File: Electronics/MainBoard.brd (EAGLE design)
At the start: 160 x 100 mm, 10 parts, among them J1 1X2-3.5MM

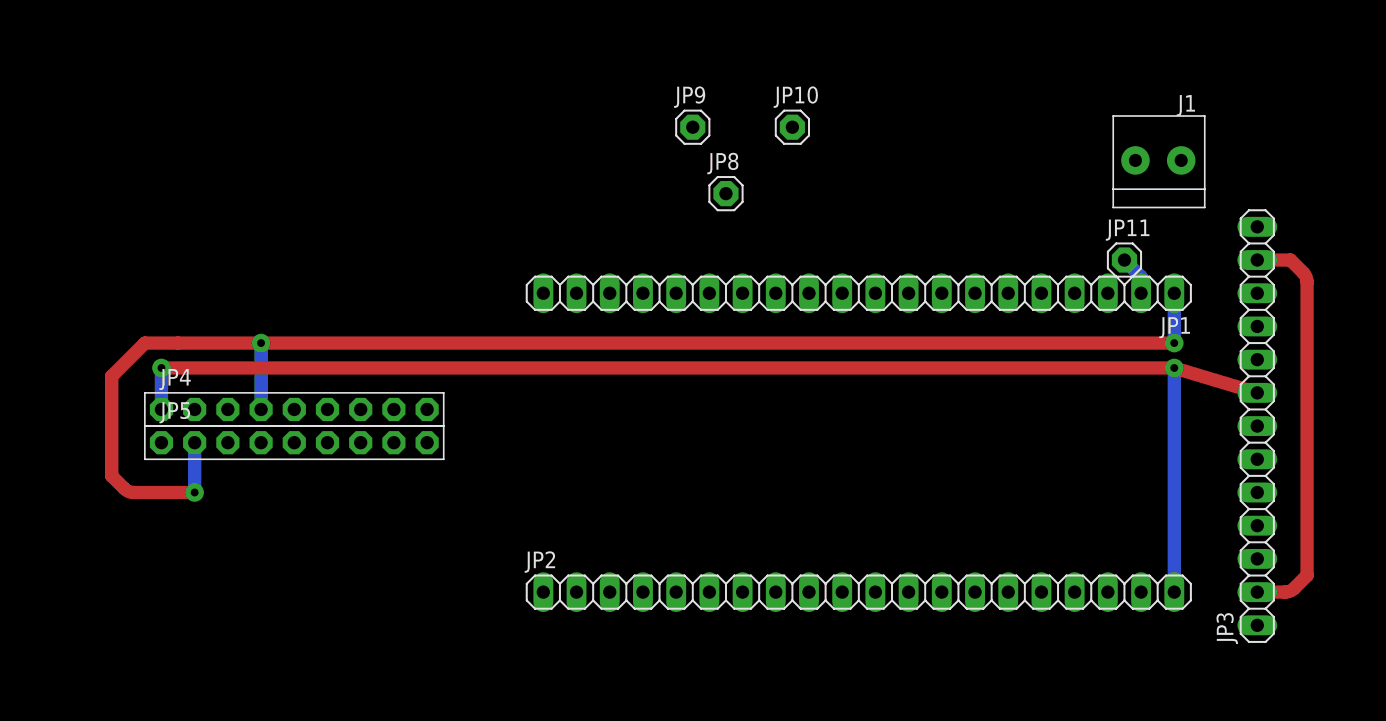
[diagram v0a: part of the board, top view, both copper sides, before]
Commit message: power routed
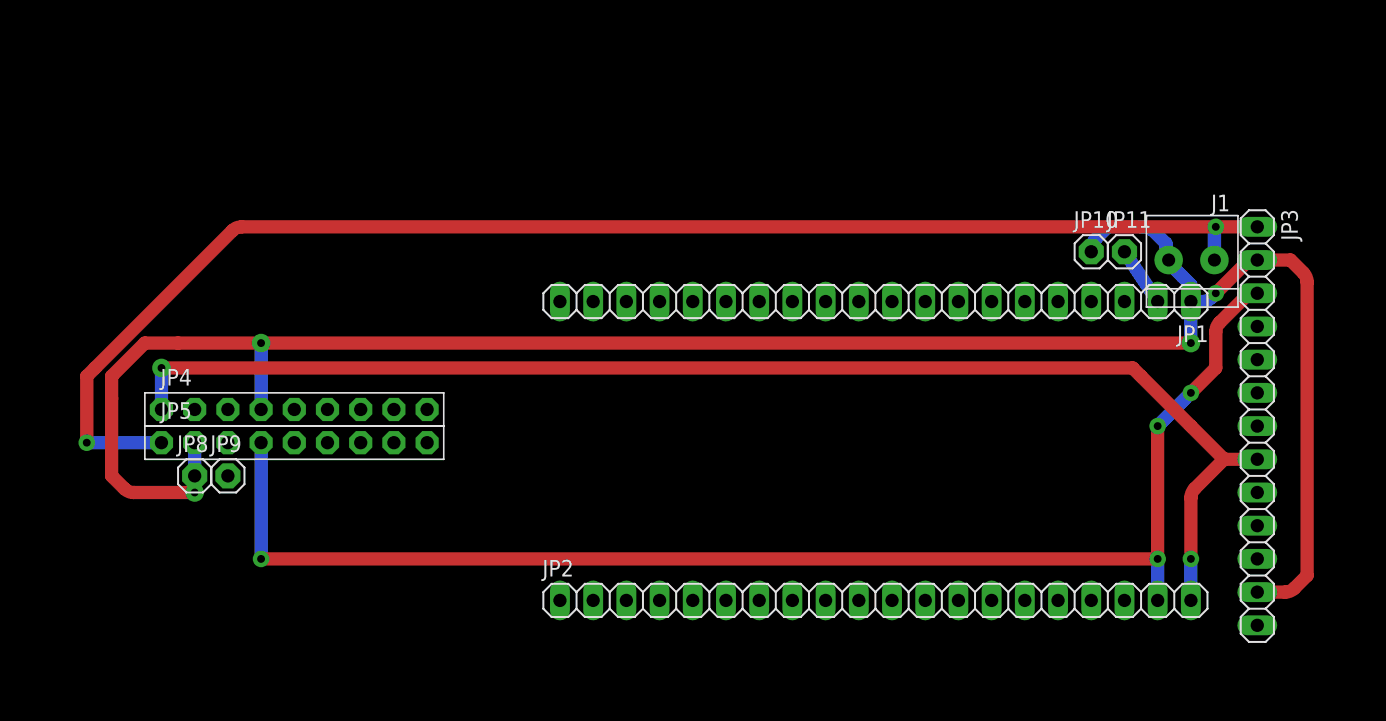
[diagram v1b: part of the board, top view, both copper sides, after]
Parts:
- moved JP8 46.0 mm to (30.5, 47.0)
- moved JP9 44.4 mm to (33.0, 47.0)
- moved JP10 24.8 mm to (99.1, 64.1)
- moved J1 8.03 mm to (106.7, 63.5)
- moved JP1 1.42 mm to (82.5, 60.3)
- moved JP2 1.42 mm to (82.5, 37.5)
- moved JP11 0.64 mm to (101.6, 64.1)
- turned JP3 to 270 degrees
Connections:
- net 8V: now also J1.1
- net GND: now also JP10.1, JP8.1
- net VIN_DIS: now also JP9.1
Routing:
- net 8V: track 0.00 -> 110.1 mm, vias 0 -> 2
- net 5V: track 0.00 -> 104.4 mm, vias 0 -> 4
- net GND: track 140.9 -> 161.5 mm, vias 3 -> 4
- net 3.3V: track 104.4 -> 101.7 mm
- net VIN: track 3.07 -> 4.58 mm

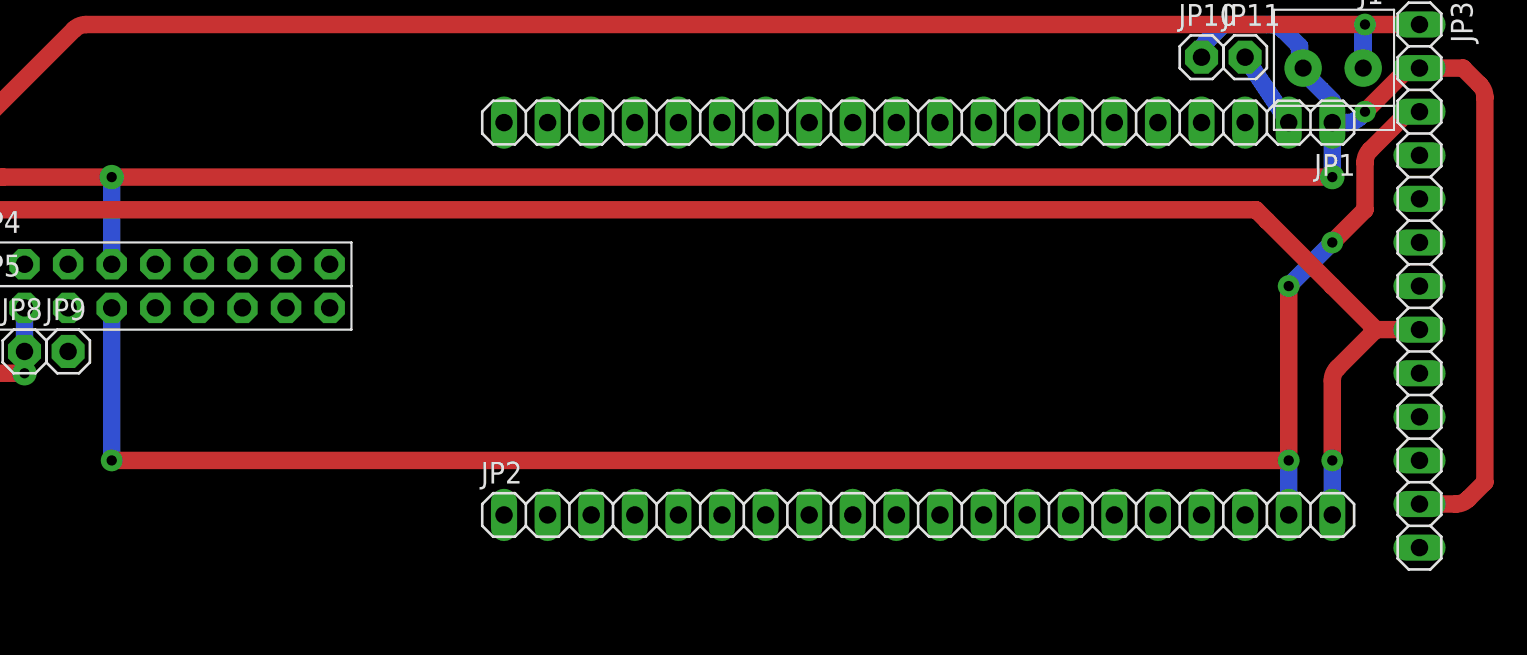
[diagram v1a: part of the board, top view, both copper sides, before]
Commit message: half routed
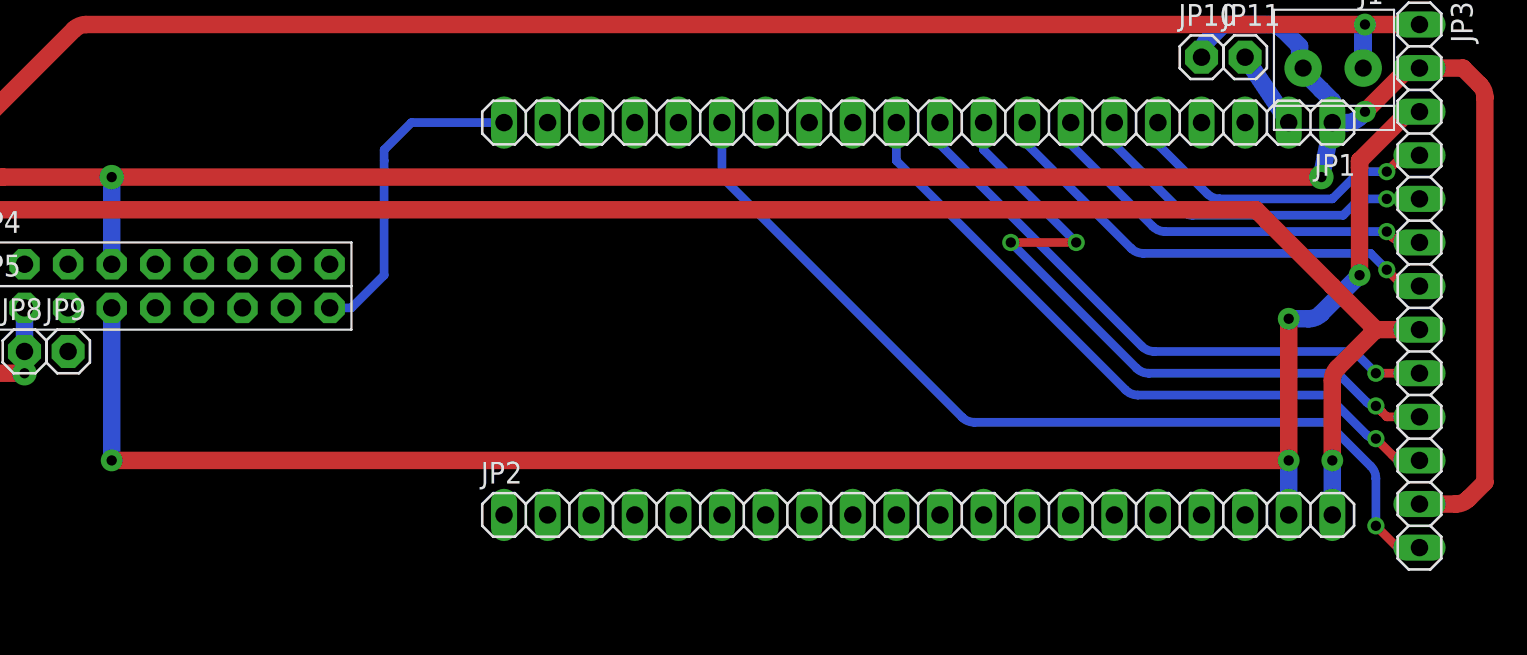
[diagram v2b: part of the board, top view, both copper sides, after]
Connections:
- net A19 renamed A_19
- removed net A15: JP1.15
- removed net A20: JP1.20
- removed net P11: JP1.11
- removed net P5: JP1.5
- removed net P6: JP1.6
- removed net P7: JP1.7
- removed net P8: JP1.8
- net G_CS_1: now also JP1.15
- net G_CS_2: now also JP1.20
- net G_DIR_1: now also JP1.6
- net G_ENCA_1: now also JP1.7
- net G_ENCB_1: now also JP1.8
- net G_INT_1: now also JP1.11
- net G_PWM_1: now also JP1.5
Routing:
- net G_CS_1: track 0.00 -> 54.5 mm, vias 0 -> 1
- net SDA: track 0.00 -> 40.9 mm, vias 0 -> 3
- net G_INT_1: track 0.00 -> 39.8 mm, vias 0 -> 1
- net SCL: track 0.00 -> 34.7 mm, vias 0 -> 1
- net G_ENCB_1: track 0.00 -> 27.4 mm, vias 0 -> 1
- net G_ENCA_1: track 0.00 -> 23.8 mm, vias 0 -> 1
- net G_DIR_1: track 0.00 -> 21.1 mm, vias 0 -> 1
- net G_CS_2: track 0.00 -> 18.9 mm
- net G_PWM_1: track 0.00 -> 18.7 mm, vias 0 -> 1
- net 5V: track 104.4 -> 105.8 mm
- net GND: track 161.5 -> 161.0 mm

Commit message: nearly done
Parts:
- added R1, R2: (no value), fab:R1206
- added U$1: USB-MINIB-5PIN, SparkFun:USB-MINIB
- moved J1 74.8 mm to (36.2, 38.4), turned to 90 degrees
- moved JP10 7.65 mm to (106.7, 63.5)
- moved JP8 6.99 mm to (37.5, 47.0)
- moved JP4 6.98 mm to (45.1, 52.1)
- moved JP5 6.98 mm to (45.1, 49.5)
- moved JP9 6.98 mm to (40.0, 47.0)
- moved JP11 2.62 mm to (104.1, 63.5)
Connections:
- removed net A16: JP1.16
- removed net G_ENC_A_2: JP5.7
- removed net G_ENC_B_2: JP5.8
- removed net P12: JP1.12
- removed net P21: JP2.1
- removed net P22: JP2.2
- removed net P23: JP2.3
- removed net P24: JP2.4
- removed net P25: JP2.5
- removed net P26: JP2.6
- removed net P29: JP2.9
- removed net P30: JP2.10
- new net A_20: JP1.20
- new net D+: JP2.11, R2.1, U$1.D+
- new net D-: JP2.12, R1.1, U$1.D-
- new net G_ENCA_2: JP2.3, JP5.7
- new net G_ENCB_2: JP2.4, JP5.8
- new net P5: JP1.5
- net GND: now also R1.2, R2.2, U$1.GND
- net G_CS_2: now also JP1.16; no longer JP1.20
- net G_DIR_2: now also JP1.12
- net G_PWM_1: now also JP2.2; no longer JP1.5
- net G_PWM_2: now also JP2.1
- net MOT_DIR: now also JP2.5
- net MOT_ENC_A: now also JP2.10
- net MOT_ENC_B: now also JP2.9
- net MOT_PWM: now also JP2.6
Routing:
- net SDA: track 40.9 -> 130.0 mm, vias 3 -> 5
- net SCL: track 34.7 -> 113.4 mm, vias 1 -> 3
- net G_PWM_1: track 18.7 -> 81.3 mm
- net D-: track 0.00 -> 57.6 mm
- net D+: track 0.00 -> 53.0 mm
- net MOT_ENC_A: track 0.00 -> 47.5 mm
- net G_DIR_2: track 0.00 -> 42.5 mm, vias 0 -> 2
- net MOT_ENC_B: track 0.00 -> 40.7 mm
- net MOT_PWM: track 0.00 -> 27.8 mm
- net G_PWM_2: track 0.00 -> 21.1 mm
- net MOT_DIR: track 0.00 -> 20.9 mm
- net G_ENCA_2: track 0.00 -> 20.6 mm
- net G_ENCB_2: track 0.00 -> 20.3 mm
- net G_CS_2: track 18.9 -> 30.7 mm, vias 0 -> 2
- net 8V: track 110.1 -> 102.3 mm
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
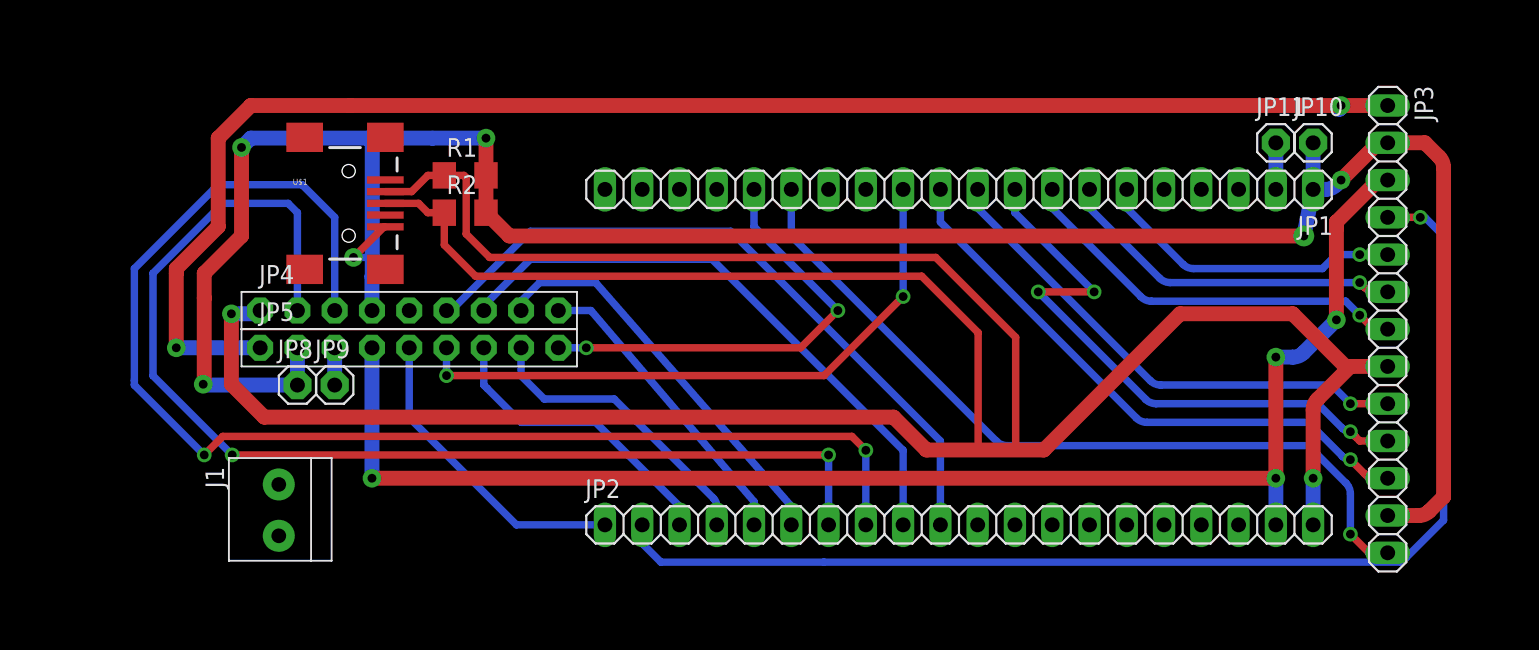
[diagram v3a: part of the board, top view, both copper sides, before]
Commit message: main board final layout v1
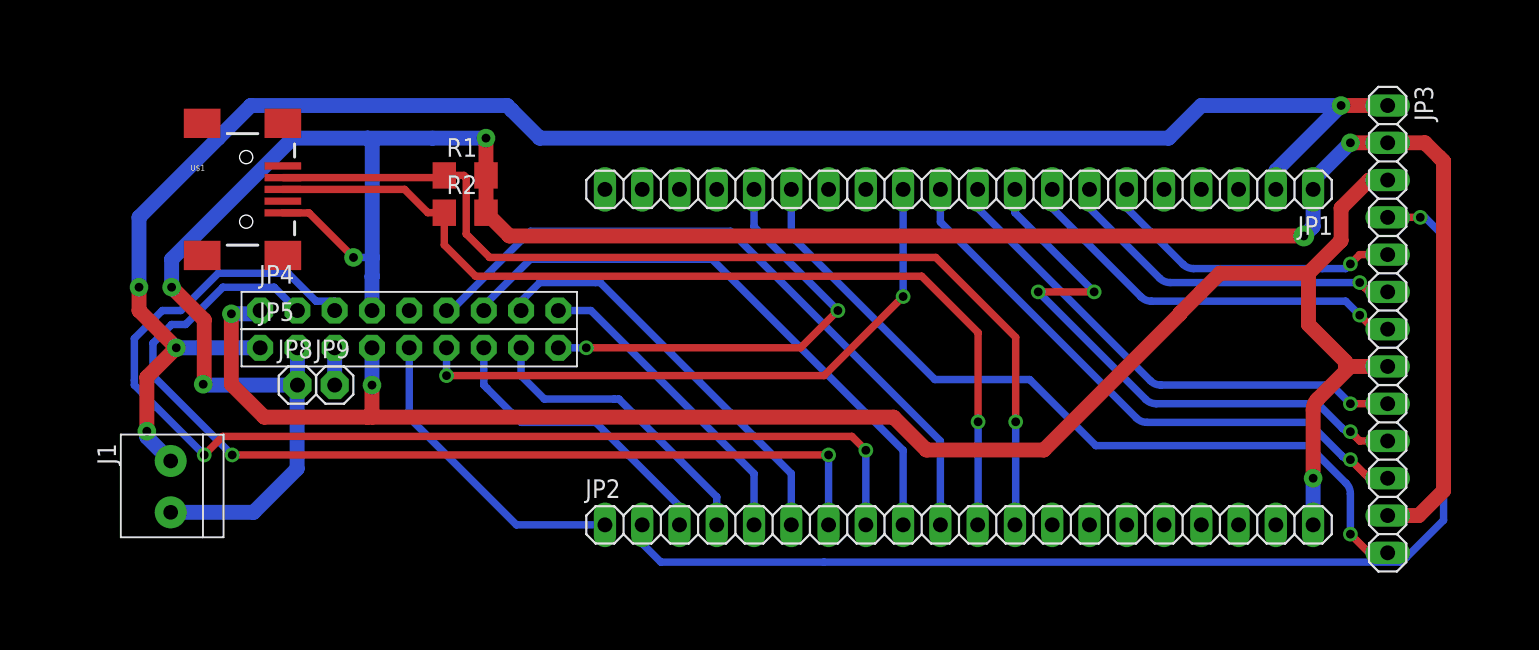
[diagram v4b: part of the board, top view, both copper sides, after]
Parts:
- removed JP10, JP11: (no value), adafruit:1X01
- moved J1 7.54 mm to (28.8, 40.0)
- moved U$1 7.05 mm to (34.0, 60.3)
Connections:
- removed net VIN: JP1.2, JP11.1
- net 3.3V: now also JP3.3, JP5.4
- net 5V: no longer JP3.3, JP5.4
- net 8V: now also JP1.2
- net GND: no longer JP10.1
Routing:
- net 5V: track 98.8 -> 0.00 mm, vias 4 -> 0
- net 8V: track 102.3 -> 122.5 mm, vias 2 -> 4
- net 3.3V: track 104.6 -> 123.4 mm, vias 2 -> 3
- net GND: track 165.7 -> 182.3 mm
- net D+: track 53.0 -> 65.8 mm, vias 0 -> 1
- net D-: track 57.6 -> 69.6 mm, vias 0 -> 1
- net SCL: track 113.4 -> 102.0 mm
- net SDA: track 130.0 -> 118.8 mm
- net VIN: track 3.17 -> 0.00 mm
- net G_ENCB_2: track 20.3 -> 21.2 mm
- net MOT_PWM: track 27.8 -> 28.5 mm
- net MOT_DIR: track 20.9 -> 21.4 mm

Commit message: mbed code
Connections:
- new net N$1: U$1.VBUS
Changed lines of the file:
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@@
 <wire x1="47.3205" y1="61.125" x2="47.473" y2="61.2775" width="0.508" layer="1"/>
+</signal>
+<signal name="N$1">
+<contactref element="U$1" pad="VBUS"/>
 </signal>
 </signals>

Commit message: main board edits
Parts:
- moved U$1 4.80 mm to (29.2, 61.0)
- moved J1 1.91 mm to (26.9, 40.0)
- moved JP4 1.91 mm to (43.2, 52.1)
- moved JP5 1.91 mm to (43.2, 49.5)
- moved JP8 1.91 mm to (35.6, 47.0)
- moved JP9 1.91 mm to (38.1, 47.0)
- moved R1 1.91 mm to (47.0, 61.3)
- moved R2 1.91 mm to (47.0, 58.7)
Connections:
- removed net N$1: U$1.VBUS
- net 5V: now also U$1.VBUS
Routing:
- net 5V: track 0.00 -> 61.0 mm
- net D-: track 69.6 -> 74.7 mm
- net GND: track 182.3 -> 187.4 mm
- net D+: track 65.8 -> 70.8 mm
- net SDA: track 118.8 -> 120.8 mm
- net MOT_PWM: track 28.5 -> 30.4 mm
- net MOT_ENC_B: track 40.7 -> 42.6 mm
- net MOT_ENC_A: track 47.5 -> 49.4 mm
- net G_PWM_2: track 21.1 -> 23.0 mm
- net G_ENCA_2: track 20.6 -> 22.5 mm
- net G_DIR_2: track 42.5 -> 44.4 mm
- net 3.3V: track 123.4 -> 125.3 mm
- net G_ENCB_2: track 21.2 -> 23.1 mm
- net MOT_DIR: track 21.4 -> 23.3 mm
- net G_CS_2: track 30.7 -> 32.6 mm
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
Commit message: board updates
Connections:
- removed net A18: JP1.18
- net G_INT_2: now also JP1.18
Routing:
- net G_INT_2: track 0.00 -> 27.0 mm
- net 8V: track 124.4 -> 123.5 mm
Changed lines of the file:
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@@
 <grid distance="0.006" unitdist="inch" unit="inch" style="lines" multiple="1" display="no" altdistance="0.025" altunitdist="inch" altunit="inch"/>
 <layers>
-<layer number="1" name="Top" color="4" fill="1" visible="no" active="yes"/>
+<layer number="1" name="Top" color="4" fill="1" visible="yes" active="yes"/>
 <layer number="2" name="Route2" color="1" fill="3" visible="no" active="no"/>
 <layer number="3" name="Route3" color="4" fill="3" visible="no" active="no"/>
@@
 <layer number="17" name="Pads" color="2" fill="1" visible="yes" active="yes"/>
 <layer number="18" name="Vias" color="2" fill="1" visible="no" active="yes"/>
-<layer number="19" name="Unrouted" color="6" fill="1" visible="no" active="yes"/>
+<layer number="19" name="Unrouted" color="6" fill="1" visible="yes" active="yes"/>
 <layer number="20" name="Dimension" color="15" fill="1" visible="no" active="yes"/>
 <layer number="21" name="tPlace" color="7" fill="1" visible="no" active="yes"/>
@@
 <layer number="45" name="Holes" color="7" fill="1" visible="no" active="yes"/>
 <layer number="46" name="Milling" color="3" fill="1" visible="no" active="yes"/>
-<layer number="47" name="Measures" color="7" fill="1" visible="no" active="yes"/>
+<layer number="47" name="Measures" color="7" fill="1" visible="yes" active="yes"/>
 <layer number="48" name="Document" color="7" fill="1" visible="no" active="yes"/>
 <layer number="49" name="Reference" color="7" fill="1" visible="no" active="yes"/>
@@
 <rectangle x1="51.1175" y1="38.4175" x2="53.34" y2="40.64" layer="1"/>
 <rectangle x1="23.3426" y1="33.655" x2="117.0051" y2="67.70793125" layer="107"/>
+<wire x1="23.3426" y1="67.70793125" x2="23.3426" y2="33.655" width="1.016" layer="47"/>
+<wire x1="23.3426" y1="33.655" x2="117.0051" y2="33.655" width="1.016" layer="47"/>
+<wire x1="117.0051" y1="33.655" x2="117.0051" y2="67.70793125" width="1.016" layer="47"/>
+<wire x1="117.0051" y1="67.70793125" x2="23.3426" y2="67.70793125" width="1.016" layer="47"/>
 </plain>
 <attributes>
@@
 <contactref element="JP1" pad="14"/>
 </signal>
-<signal name="A18">
-<contactref element="JP1" pad="18"/>
-</signal>
 <signal name="3.3V">
 <contactref element="JP2" pad="20"/>
@@
 <wire x1="104.14" y1="61.595" x2="108.585" y2="66.04" width="1.016" layer="16"/>
 <wire x1="108.585" y1="66.04" x2="99.06" y2="66.04" width="1.016" layer="16"/>
-<wire x1="99.06" y1="66.04" x2="96.8375" y2="63.8175" width="1.016" layer="16"/>
-<wire x1="96.8375" y1="63.8175" x2="52.07" y2="63.8175" width="1.016" layer="16"/>
-<wire x1="52.07" y1="63.8175" x2="50.165" y2="65.7225" width="1.016" layer="16"/>
-<wire x1="50.165" y1="65.7225" x2="49.8475" y2="66.04" width="1.016" layer="16"/>
 <wire x1="49.8475" y1="66.04" x2="32.385" y2="66.04" width="1.016" layer="16"/>
 <wire x1="32.385" y1="66.04" x2="30.1625" y2="63.8175" width="1.016" layer="16"/>
@@
 <wire x1="25.2984" y1="43.84548125" x2="25.2984" y2="43.4433" width="1.016" layer="16"/>
 <wire x1="25.2984" y1="43.4433" x2="26.924" y2="41.8177" width="1.016" layer="16"/>
+<wire x1="99.06" y1="66.04" x2="99.06" y2="65.9892" width="1.016" layer="16"/>
+<wire x1="99.06" y1="65.9892" x2="97.9932" y2="64.9224" width="1.016" layer="16"/>
+<wire x1="97.9932" y1="64.9224" x2="50.9651" y2="64.9224" width="1.016" layer="16"/>
+<wire x1="50.9651" y1="64.9224" x2="49.8475" y2="66.04" width="1.016" layer="16"/>
 </signal>
 <signal name="G_PWM_1">
@@
 <signal name="G_INT_2">
 <contactref element="JP4" pad="5"/>
+<contactref element="JP1" pad="18"/>
+<wire x1="43.18" y1="52.07" x2="43.18" y2="52.7812" width="0.508" layer="16"/>
+<wire x1="43.18" y1="52.7812" x2="52.1208" y2="61.722" width="0.508" layer="16"/>
+<wire x1="52.1208" y1="61.722" x2="53.1876" y2="62.7888" width="0.508" layer="16"/>
+<wire x1="53.1876" y1="62.7888" x2="62.3316" y2="62.7888" width="0.508" layer="16"/>
+<wire x1="62.3316" y1="62.7888" x2="63.3984" y2="61.722" width="0.508" layer="16"/>
+<wire x1="63.3984" y1="61.722" x2="63.3984" y2="60.4266" width="0.508" layer="16"/>
+<wire x1="63.3984" y1="60.4266" x2="63.5" y2="60.325" width="0.508" layer="16"/>
 </signal>
 <signal name="G_CS_2">
